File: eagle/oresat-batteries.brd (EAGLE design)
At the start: 99.8 x 94.6 mm, 308 parts, among them J1 J-SAMTEC-TFM-120-X1-XXX-D-RA, J4 ORESAT-DEBUG-CONNECTOR-ALL, Q1 DMP2240UDM, Q10 NTR4101, Q11 PMV45EN, Q12 Si7625DN, Q13 Si7625DN, Q14 NTR4101, Q15 NTR4101, Q16 Si7625DN, Q17 Si7625DN, Q18 Si7625DN, Q19 Si7625DN, Q2 PMV45EN, Q22 PMV45EN, Q23 NTR4101, Q24 PM45VEN, Q25 PM45VEN, Q26 PM45VEN, Q27 PM45VEN, Q28 NTR4101, Q29 PM45VEN, Q3 DMP3050LVT-7, Q30 Si7625DN, Q31 Si7625DN, Q32 NTR4101, Q33 NTR4101, Q34 Si7625DN, Q35 Si7625DN, Q36 Si7625DN, Q37 Si7625DN, Q4 DMP3050LVT-7, Q40 PM45VEN, Q41 NTR4101, Q42 DMP2240UDM, Q43 DMP2240UDM, Q44 PMV45EN, Q45 FDMQ86530L_2-GATES, Q5 PMV45EN, Q6 PM45VEN, Q7 PM45VEN, Q8 PM45VEN, Q9 PM45VEN, U1 MAX7310ATE, U10 LTC4412, U11 LTC4412, U12 MAX17205G, U13 S-8209AAA-T8T1U, U14 S-8209AAA-T8T1U, U15 LTC4412, U16 LTC4412, U17 MAX17205G, U2 MIC842LYC5, U20 TCAN330, U21 STM32F091C, U3 MIC842LYC5, U4 MAX4211FETE, U5 TPS62111RSA, U8 S-8209AAA-T8T1U, U9 S-8209AAA-T8T1U, X3 16MHZ-2.5x2mm

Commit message: Full update of the BOM; added non PCB materials including the heaters, thermistors. Updated fuses to be decent PTCs. Might regret that later, but it really seems like the right thing.
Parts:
- C7: value NP -> 1u
- F1, F2: value GENERIC-FUSE-1206 -> 1206L500/12SLPR
- F3, F4: value GENERIC-FUSE-1206 -> 1206L150/12SLYR
- R26: value NP -> 100k
- R27: value NP -> 10k
- R88, R89: value 1M -> 10k
- R90, R91: value 1M -> 100k
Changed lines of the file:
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@@
 <attribute name="NAME" x="85.1" y="42" size="0.635" layer="26" font="vector" ratio="20" rot="MR0"/>
 </element>
-<element name="F1" library="F-Generic-Fuse-1206" package="1206-C" value="GENERIC-FUSE-1206" x="76.5" y="39.9" smashed="yes">
+<element name="F1" library="F-Generic-Fuse-1206" package="1206-C" value="1206L500/12SLPR" x="76.5" y="39.9" smashed="yes">
 <attribute name="DIS" value="Digi-Key" x="76.5" y="39.9" size="1.778" layer="27" display="off"/>
 <attribute name="DPN" value="F9966CT-ND" x="76.5" y="39.9" size="1.778" layer="27" display="off"/>
@@
 <attribute name="NAME" x="65.6" y="65.1" size="0.635" layer="25" font="vector" ratio="20"/>
 </element>
-<element name="R91" library="oresat-rcl" package=".0603-C-NOSILK" value="1M" x="20.3" y="67.6" smashed="yes" rot="R270">
+<element name="R91" library="oresat-rcl" package=".0603-C-NOSILK" value="100k" x="20.3" y="67.6" smashed="yes" rot="R270">
 <attribute name="DIS" value="Digi-Key" x="20.3" y="67.6" size="1.778" layer="27" rot="R270" display="off"/>
 <attribute name="DPN" value="311-1.00MHRCT-ND" x="20.3" y="67.6" size="1.778" layer="27" rot="R270" display="off"/>
@@
 <attribute name="VALUE" x="18.95" y="68.4" size="0.8" layer="27" font="vector" ratio="15" rot="R270"/>
 </element>
-<element name="R90" library="oresat-rcl" package=".0603-C-NOSILK" value="1M" x="87.4" y="75.4" smashed="yes" rot="R270">
+<element name="R90" library="oresat-rcl" package=".0603-C-NOSILK" value="100k" x="87.4" y="75.4" smashed="yes" rot="R270">
 <attribute name="DIS" value="Digi-Key" x="87.4" y="75.4" size="1.778" layer="27" rot="R270" display="off"/>
 <attribute name="DPN" value="311-1.00MHRCT-ND" x="87.4" y="75.4" size="1.778" layer="27" rot="R270" display="off"/>
@@
 <attribute name="VALUE" x="86.7" y="85.28" size="0.8" layer="27" font="vector" ratio="15"/>
 </element>
-<element name="R89" library="oresat-rcl" package=".0603-C-NOSILK" value="1M" x="21.6" y="72.4" smashed="yes">
+<element name="R89" library="oresat-rcl" package=".0603-C-NOSILK" value="10k" x="21.6" y="72.4" smashed="yes">
 <attribute name="DIS" value="Digi-Key" x="21.6" y="72.4" size="1.778" layer="27" display="off"/>
 <attribute name="DPN" value="311-1.00MHRCT-ND" x="21.6" y="72.4" size="1.778" layer="27" display="off"/>
@@
 <attribute name="VALUE" x="20.8" y="71.05" size="0.8" layer="27" font="vector" ratio="15"/>
 </element>
-<element name="R88" library="oresat-rcl" package=".0603-C-NOSILK" value="1M" x="88" y="86.3" smashed="yes" rot="R180">
+<element name="R88" library="oresat-rcl" package=".0603-C-NOSILK" value="10k" x="88" y="86.3" smashed="yes" rot="R180">
 <attribute name="DIS" value="Digi-Key" x="88" y="86.3" size="1.778" layer="27" rot="R180" display="off"/>
 <attribute name="DPN" value="311-1.00MHRCT-ND" x="88" y="86.3" size="1.778" layer="27" rot="R180" display="off"/>
@@
 <attribute name="NAME" x="85.2" y="81.7" size="0.635" layer="26" font="vector" ratio="20" rot="MR0"/>
 </element>
-<element name="F2" library="F-Generic-Fuse-1206" package="1206-C" value="GENERIC-FUSE-1206" x="76.4" y="78.6" smashed="yes">
+<element name="F2" library="F-Generic-Fuse-1206" package="1206-C" value="1206L500/12SLPR" x="76.4" y="78.6" smashed="yes">
 <attribute name="DIS" value="Digi-Key" x="76.4" y="78.6" size="1.778" layer="27" display="off"/>
 <attribute name="DPN" value="F9966CT-ND" x="76.4" y="78.6" size="1.778" layer="27" display="off"/>
@@
 <attribute name="VALUE" x="40.65" y="69.3" size="0.8" layer="27" font="vector" ratio="15" rot="R90"/>
 </element>
-<element name="R26" library="oresat-rcl" package=".0603-C-NOSILK" value="NP" x="40" y="61" smashed="yes" rot="R180">
+<element name="R26" library="oresat-rcl" package=".0603-C-NOSILK" value="100k" x="40" y="61" smashed="yes" rot="R180">
 <attribute name="DIS" value="Digi-Key" x="40" y="61" size="1.778" layer="27" rot="R180" display="off"/>
 <attribute name="DPN" value="1276-4275-1-ND" x="40" y="61" size="1.778" layer="27" rot="R180" display="off"/>
@@
 <attribute name="VALUE" x="40.8" y="62.35" size="0.8" layer="27" font="vector" ratio="15" rot="R180"/>
 </element>
-<element name="R27" library="oresat-rcl" package=".0603-C-NOSILK" value="NP" x="40" y="62.1" smashed="yes" rot="R180">
+<element name="R27" library="oresat-rcl" package=".0603-C-NOSILK" value="10k" x="40" y="62.1" smashed="yes" rot="R180">
 <attribute name="DIS" value="Digi-Key" x="40" y="62.1" size="1.778" layer="27" rot="R180" display="off"/>
 <attribute name="DPN" value="1276-4275-1-ND" x="40" y="62.1" size="1.778" layer="27" rot="R180" display="off"/>
@@
 <attribute name="VALUE" x="40.8" y="63.45" size="0.8" layer="27" font="vector" ratio="15" rot="R180"/>
 </element>
-<element name="C7" library="oresat-rcl" package=".0603-C-NOSILK" value="NP" x="38.7" y="63.2" smashed="yes" rot="R180">
+<element name="C7" library="oresat-rcl" package=".0603-C-NOSILK" value="1u" x="38.7" y="63.2" smashed="yes" rot="R180">
 <attribute name="NAME" x="38.7" y="63.2" size="0.2" layer="33" ratio="15" rot="R180" align="center"/>
 <attribute name="NAME" x="37.8" y="63.85" size="0.635" layer="25" font="vector" ratio="20"/>
@@
 <attribute name="VALUE" x="49.75" y="28.4" size="0.8" layer="27" font="vector" ratio="15" rot="R90"/>
 </element>
-<element name="F3" library="F-Generic-Fuse-1206" package="1206-C" value="GENERIC-FUSE-1206" x="72.2" y="36" smashed="yes">
+<element name="F3" library="F-Generic-Fuse-1206" package="1206-C" value="1206L150/12SLYR" x="72.2" y="36" smashed="yes">
 <attribute name="DIS" value="Digi-Key" x="72.2" y="36" size="1.778" layer="27" display="off"/>
 <attribute name="DPN" value="F9966CT-ND" x="72.2" y="36" size="1.778" layer="27" display="off"/>
@@
 </element>
 <element name="PCB1" library="oresat-cards" package="ORESAT-CARD-V1.3-BATTERY" value="ORESAT-CARD-V1.3-BATTERY" x="0" y="0" locked="yes" smashed="yes"/>
-<element name="F4" library="F-Generic-Fuse-1206" package="1206-C" value="GENERIC-FUSE-1206" x="72.1" y="74.7" smashed="yes">
+<element name="F4" library="F-Generic-Fuse-1206" package="1206-C" value="1206L150/12SLYR" x="72.1" y="74.7" smashed="yes">
 <attribute name="DIS" value="Digi-Key" x="72.1" y="74.7" size="1.778" layer="27" display="off"/>
 <attribute name="DPN" value="F9966CT-ND" x="72.1" y="74.7" size="1.778" layer="27" display="off"/>

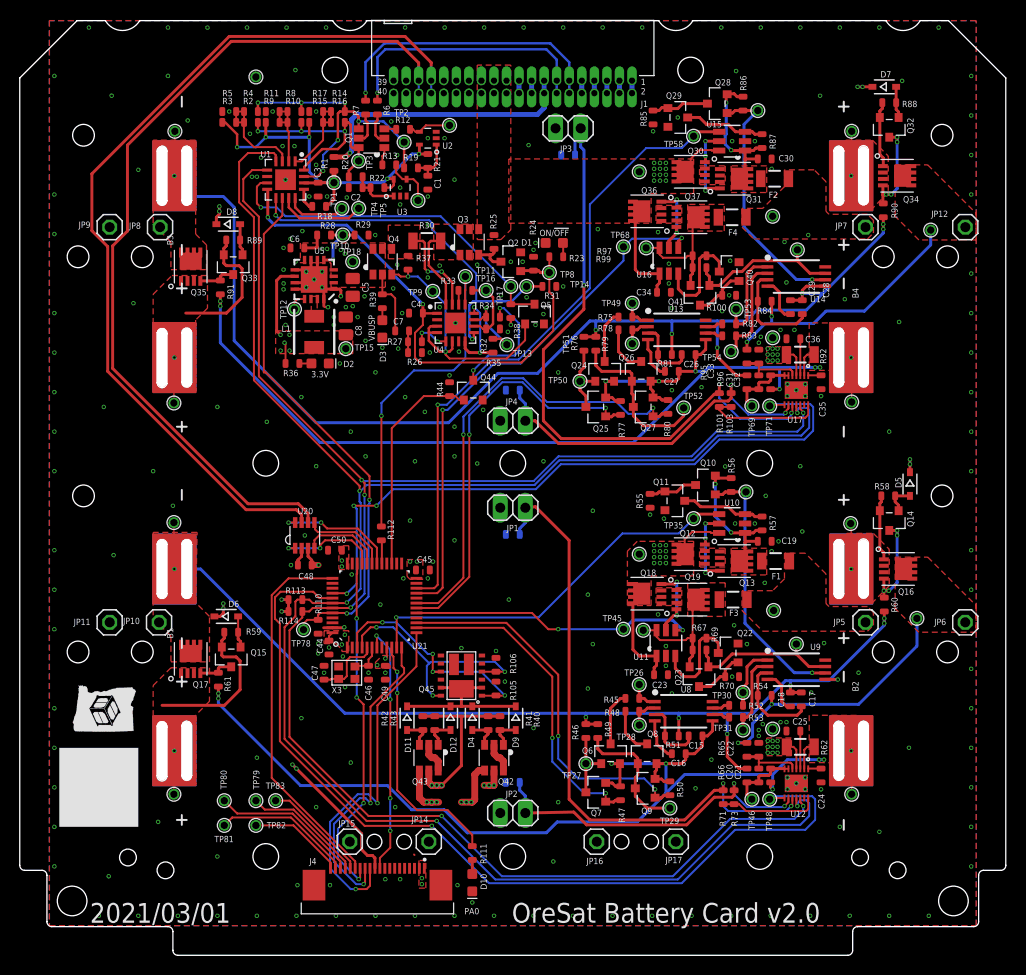
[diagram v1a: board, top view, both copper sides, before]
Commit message: Upped battery board to v2.1. No real changes, besides adding fiducials (blargh!), updating the board version, and adding the flight marker to TPLACE.
More importantly, the BOM has been upadated to reflect what Screaming Circuits is going to stuff for us.
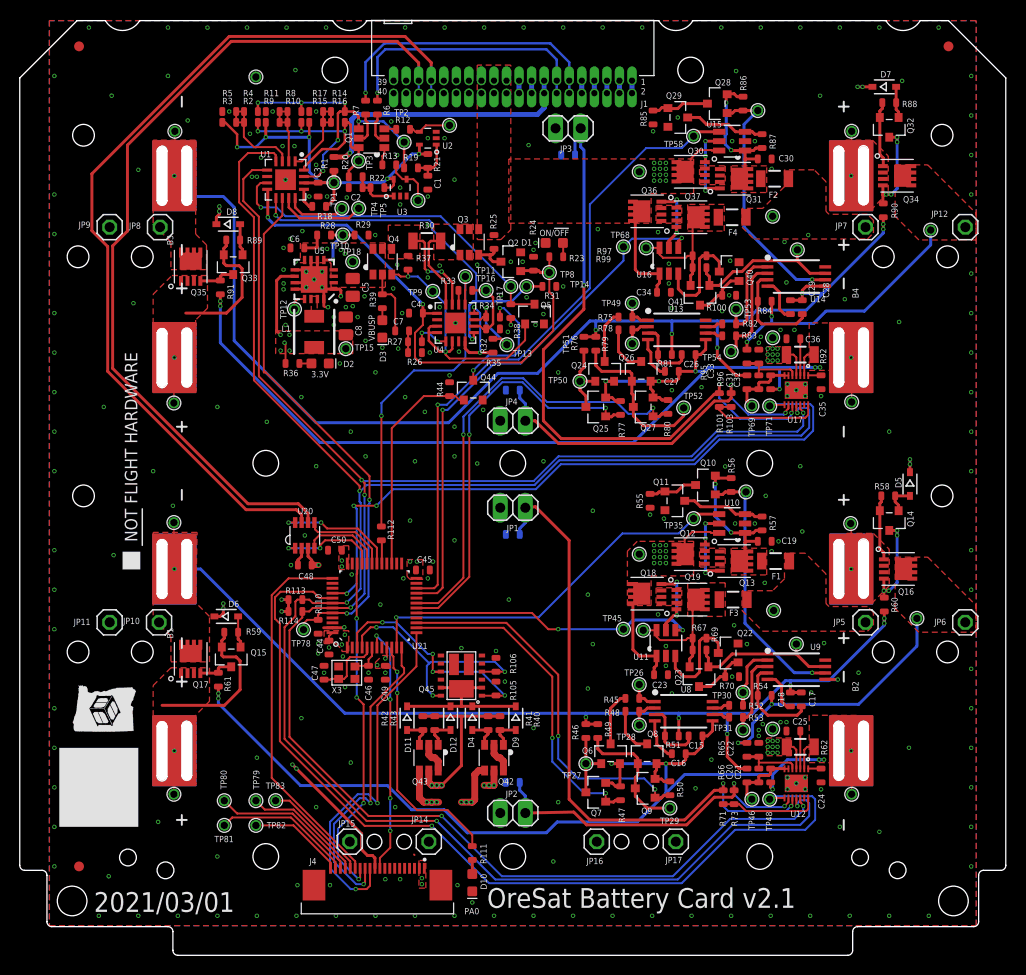
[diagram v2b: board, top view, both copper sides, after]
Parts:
- added FIDUCIAL1, FIDUCIAL2, FIDUCIAL3: FIDUCIAL-1.0X2.0, dock_v2:FIDUCIAL-1.0X2.0
- added U$1: FLIGHMARKERNEW, oresat-flight-marker:FLIGHTMARKER_NEW_BOARDS
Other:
- board text added: "OreSat Battery Card v2.1"
- board text removed: "OreSat Battery Card v2.0"
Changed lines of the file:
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@@
 <board>
 <plain>
-<text x="49.8" y="3.3" size="2" layer="21" font="vector" ratio="15">OreSat Battery Card v2.0</text>
-<text x="7.1058" y="3.2934" size="2" layer="21" font="vector" ratio="15">2021/03/01</text>
+<text x="47.3" y="4.8" size="2" layer="21" font="vector" ratio="15">OreSat Battery Card v2.1</text>
+<text x="7.5058" y="4.3934" size="2" layer="21" font="vector" ratio="15">2021/03/01</text>
 <rectangle x1="7.3639" y1="22.6149" x2="7.3893" y2="22.6403" layer="21"/>
 <rectangle x1="7.4147" y1="22.6149" x2="7.4655" y2="22.6403" layer="21"/>
@@
 <attribute name="DPN" value="RC0603JR-071KL" x="62" y="24.7" size="1.778" layer="27" display="off"/>
 <attribute name="MPN" value="311-1.0KGRCT-ND" x="62" y="24.7" size="1.778" layer="27" display="off"/>
-<attribute name="NAME" x="59.2" y="24.25" size="0.635" layer="25" font="vector" ratio="20"/>
 <attribute name="NAME" x="62" y="24.7" size="0.2" layer="33" ratio="15" align="center"/>
+<attribute name="NAME" x="59.2" y="24.25" size="0.635" layer="25" font="vector" ratio="20"/>
 <attribute name="VALUE" x="61.2" y="23.35" size="0.8" layer="27" font="vector" ratio="15"/>
 </element>
@@
 <attribute name="MFR" value="Vishay" x="20.9" y="34.3" size="1.778" layer="27" display="off"/>
 <attribute name="MPN" value="1N4151WS-E3-08" x="20.9" y="34.3" size="1.778" layer="27" display="off"/>
-<attribute name="NAME" x="21.1" y="35.25" size="0.635" layer="25" font="vector" ratio="20"/>
 <attribute name="NAME" x="20.9" y="34.3" size="0.2" layer="33" ratio="15" align="center"/>
+<attribute name="NAME" x="21.1" y="35.25" size="0.635" layer="25" font="vector" ratio="20"/>
 <attribute name="POPULARITY" value="4" x="20.9" y="34.3" size="1.778" layer="27" display="off"/>
 <attribute name="VALUE" x="20.1" y="31.68" size="0.8" layer="27" font="vector" ratio="15"/>
@@
 <attribute name="MFR" value="Vishay" x="90.1" y="47.7" size="1.778" layer="27" rot="R270" display="off"/>
 <attribute name="MPN" value="1N4151WS-E3-08" x="90.1" y="47.7" size="1.778" layer="27" rot="R270" display="off"/>
-<attribute name="NAME" x="89.25" y="47.3" size="0.635" layer="25" font="vector" ratio="20" rot="R90"/>
 <attribute name="NAME" x="90.1" y="47.7" size="0.2" layer="33" ratio="15" rot="R270" align="center"/>
+<attribute name="NAME" x="89.25" y="47.3" size="0.635" layer="25" font="vector" ratio="20" rot="R90"/>
 <attribute name="POPULARITY" value="4" x="90.1" y="47.7" size="1.778" layer="27" rot="R270" display="off"/>
 <attribute name="VALUE" x="87.48" y="48.5" size="0.8" layer="27" font="vector" ratio="15" rot="R270"/>
@@
 <attribute name="DPN" value="RC0603JR-071KL" x="62" y="26" size="1.778" layer="27" display="off"/>
 <attribute name="MPN" value="311-1.0KGRCT-ND" x="62" y="26" size="1.778" layer="27" display="off"/>
-<attribute name="NAME" x="59.1" y="25.55" size="0.635" layer="25" font="vector" ratio="20"/>
 <attribute name="NAME" x="62" y="26" size="0.2" layer="33" ratio="15" align="center"/>
+<attribute name="NAME" x="59.1" y="25.55" size="0.635" layer="25" font="vector" ratio="20"/>
 <attribute name="VALUE" x="61.3" y="24.75" size="0.8" layer="27" font="vector" ratio="15"/>
 </element>
@@
 <attribute name="MFR" value="Kemet" x="66" y="59.1" size="1.778" layer="27" display="off"/>
 <attribute name="MPN" value="C0603C103M5RACTU" x="66" y="59.1" size="1.778" layer="27" display="off"/>
-<attribute name="NAME" x="66" y="59.1" size="0.2" layer="33" ratio="15" align="center"/>
 <attribute name="NAME" x="65.2" y="57.75" size="0.635" layer="25" font="vector" ratio="20"/>
+<attribute name="NAME" x="66" y="59.1" size="0.2" layer="33" ratio="15" align="center"/>
 <attribute name="VALUE" x="65.2" y="57.75" size="0.8" layer="27" font="vector" ratio="15"/>
 </element>
@@
 <attribute name="MFR" value="Vishay" x="21.1" y="74" size="1.778" layer="27" display="off"/>
 <attribute name="MPN" value="1N4151WS-E3-08" x="21.1" y="74" size="1.778" layer="27" display="off"/>
-<attribute name="NAME" x="20.9" y="74.95" size="0.635" layer="25" font="vector" ratio="20"/>
 <attribute name="NAME" x="21.1" y="74" size="0.2" layer="33" ratio="15" align="center"/>
+<attribute name="NAME" x="20.9" y="74.95" size="0.635" layer="25" font="vector" ratio="20"/>
 <attribute name="POPULARITY" value="4" x="21.1" y="74" size="1.778" layer="27" display="off"/>
 <attribute name="VALUE" x="20.3" y="71.38" size="0.8" layer="27" font="vector" ratio="15"/>
@@
 <attribute name="MFR" value="Vishay" x="87.5" y="87.9" size="1.778" layer="27" display="off"/>
 <attribute name="MPN" value="1N4151WS-E3-08" x="87.5" y="87.9" size="1.778" layer="27" display="off"/>
-<attribute name="NAME" x="87.1" y="88.85" size="0.635" layer="25" font="vector" ratio="20"/>
 <attribute name="NAME" x="87.5" y="87.9" size="0.2" layer="33" ratio="15" align="center"/>
+<attribute name="NAME" x="87.1" y="88.85" size="0.635" layer="25" font="vector" ratio="20"/>
 <attribute name="POPULARITY" value="4" x="87.5" y="87.9" size="1.778" layer="27" display="off"/>
 <attribute name="VALUE" x="86.7" y="85.28" size="0.8" layer="27" font="vector" ratio="15"/>
@@
 <attribute name="VALUE" x="71.3" y="72.5" size="1" layer="27" ratio="10"/>
 </element>
+<element name="FIDUCIAL1" library="dock_v2" package="FIDUCIAL-1.0X2.0" value="FIDUCIAL-1.0X2.0" x="94" y="92" smashed="yes"/>
+<element name="FIDUCIAL2" library="dock_v2" package="FIDUCIAL-1.0X2.0" value="FIDUCIAL-1.0X2.0" x="6" y="92" smashed="yes"/>
+<element name="FIDUCIAL3" library="dock_v2" package="FIDUCIAL-1.0X2.0" value="FIDUCIAL-1.0X2.0" x="6" y="9" smashed="yes"/>
+<element name="U$1" library="oresat-flight-marker" package="FLIGHTMARKER_NEW_BOARDS" value="FLIGHMARKERNEW" x="11.9" y="39.3" smashed="yes" rot="R90"/>
 </elements>
 <signals>

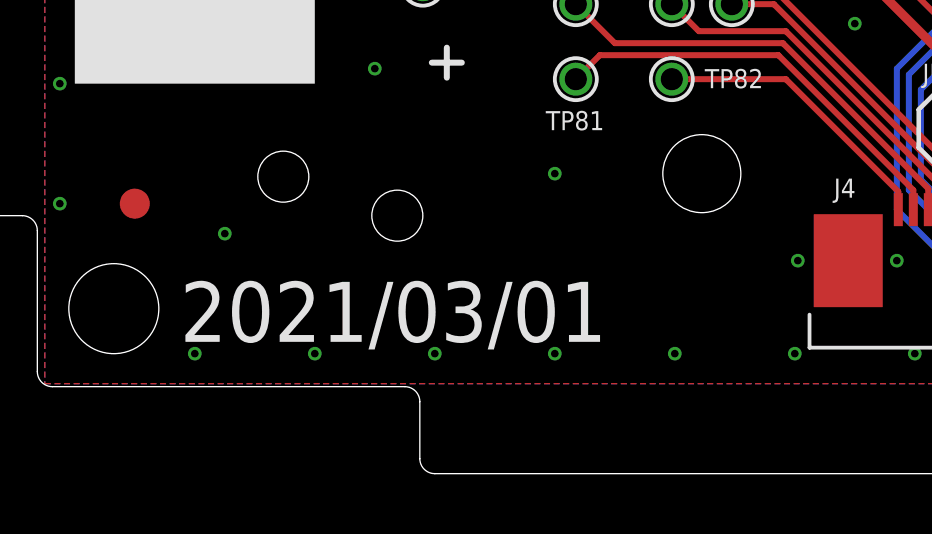
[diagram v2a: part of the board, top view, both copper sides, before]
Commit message: Updated shutdown mosfet resistors to 100k after the battery failed quiescent power draw, and removed backup thermistors from the BOM.
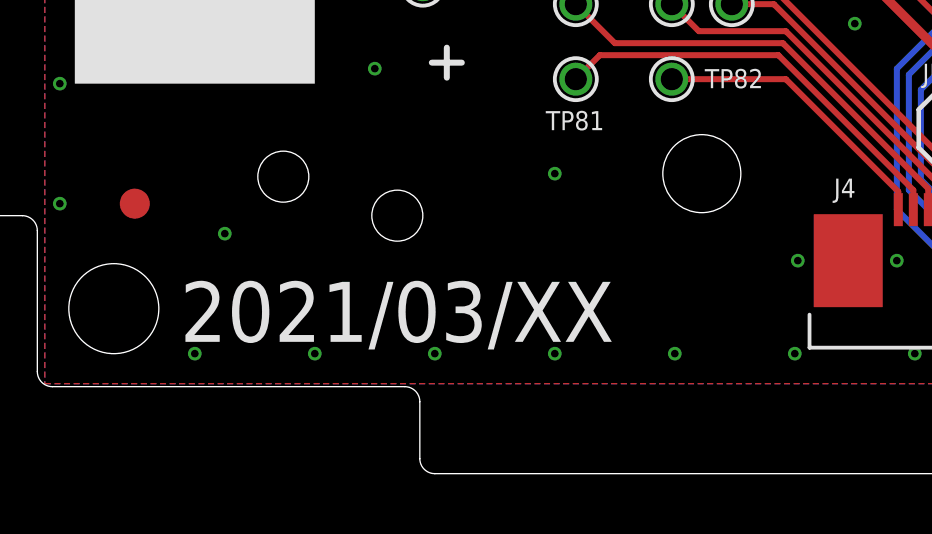
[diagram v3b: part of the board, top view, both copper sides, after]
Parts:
- R102, R104, R72, R74: value 10k -> NP
- R58, R59, R88, R89: value 10k -> 100k
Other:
- board text added: "2021/03/XX"
- board text removed: "2021/03/01"
